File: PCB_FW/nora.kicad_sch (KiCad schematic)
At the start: 269 parts, among them J1 USB_C_Receptacle_USB2.0, J2 Conn_01x04, J3 Conn_01x02, J4 Conn_01x02, J5 Conn_02x03_Odd_Even, U1 ATmega32U4-MU, U2 24LC64, U4 Pico, Y1 16MHz

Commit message: フットプリントを整理
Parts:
- SW_1, SW_3: footprint Keebio-Parts:Kailh-PG1350-1u-MBK-WithKeyName-Socket-ForLeftEdge2 -> Keebio-Parts:Kailh-PG1350-1u-MBK-WithKeyName-Socket-ForLeftEdge
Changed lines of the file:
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@@
     (property "Reference" "SW_1" (id 0) (at 29.845 30.861 0))
     (property "Value" "ESC" (id 1) (at 29.845 33.1724 0))
-    (property "Footprint" "Keebio-Parts:Kailh-PG1350-1u-MBK-WithKeyName-Socket-ForLeftEdge2" (id 2) (at 29.845 33.02 0)
+    (property "Footprint" "Keebio-Parts:Kailh-PG1350-1u-MBK-WithKeyName-Socket-ForLeftEdge" (id 2) (at 29.845 33.02 0)
       (effects (font (size 1.27 1.27)) hide)
     )
@@
     (property "Reference" "SW_3" (id 0) (at 29.845 95.631 0))
     (property "Value" "LSFT" (id 1) (at 29.845 97.9424 0))
-    (property "Footprint" "Keebio-Parts:Kailh-PG1350-1u-MBK-WithKeyName-Socket-ForLeftEdge2" (id 2) (at 29.845 97.79 0)
+    (property "Footprint" "Keebio-Parts:Kailh-PG1350-1u-MBK-WithKeyName-Socket-ForLeftEdge" (id 2) (at 29.845 97.79 0)
       (effects (font (size 1.27 1.27)) hide)
     )
@@
     )
     (path "/00000000-0000-0000-0000-00005f6b0365"
-      (reference "SW_1") (unit 1) (value "ESC") (footprint "Keebio-Parts:Kailh-PG1350-1u-MBK-WithKeyName-Socket-ForLeftEdge2")
+      (reference "SW_1") (unit 1) (value "ESC") (footprint "Keebio-Parts:Kailh-PG1350-1u-MBK-WithKeyName-Socket-ForLeftEdge")
     )
     (path "/00000000-0000-0000-0000-000061ad1b1e"
-      (reference "SW_3") (unit 1) (value "LSFT") (footprint "Keebio-Parts:Kailh-PG1350-1u-MBK-WithKeyName-Socket-ForLeftEdge2")
+      (reference "SW_3") (unit 1) (value "LSFT") (footprint "Keebio-Parts:Kailh-PG1350-1u-MBK-WithKeyName-Socket-ForLeftEdge")
     )
     (path "/00000000-0000-0000-0000-000061aaf91e"

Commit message: Enlarge SW sub-hole? #68
1.7mmから1.8mmへ、5ピンの穴サイズを拡大
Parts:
- SW_1, SW_3: footprint Keebio-Parts:Kailh-PG1350-1u-MBK-WithKeyName-Socket-ForLeftEdge -> Keebio-Parts:Kailh-PG1350-1u-MBK-WithKeyName-Socket-ForLeftEdge-1.8mm-hole
- SW_10, SW_11, SW_12, SW_13, SW_15, SW_16, SW_17, SW_18, SW_20, SW_21, SW_22, SW_23, SW_24, SW_25, SW_26, SW_27, SW_28, SW_30, SW_31, SW_32, SW_33, SW_35, SW_36, SW_37, SW_38, SW_39, SW_40, SW_41, SW_42, SW_43, SW_44, SW_45, SW_46, SW_47, SW_48, SW_49, SW_5, SW_50, SW_51, SW_52, SW_53, SW_55, SW_56, SW_57, SW_58, SW_59, SW_60, SW_61, SW_62, SW_63, SW_65, SW_66, SW_67, SW_68, SW_70, SW_71, SW_72, SW_73, SW_75, SW_78, SW_8: footprint Keebio-Parts:Kailh-PG1350-1u-MBK-WithKeyName-Socket -> Keebio-Parts:Kailh-PG1350-1u-MBK-WithKeyName-Socket-1.8mm-hole
- SW_19, SW_29, SW_54, SW_6, SW_64, SW_7, SW_76, SW_77: footprint Keebio-Parts:Kailh-PG1350-1.5u-MBK-WithKeyName-Socket -> Keebio-Parts:Kailh-PG1350-1.5u-MBK-WithKeyName-Socket-1.8mm-hole

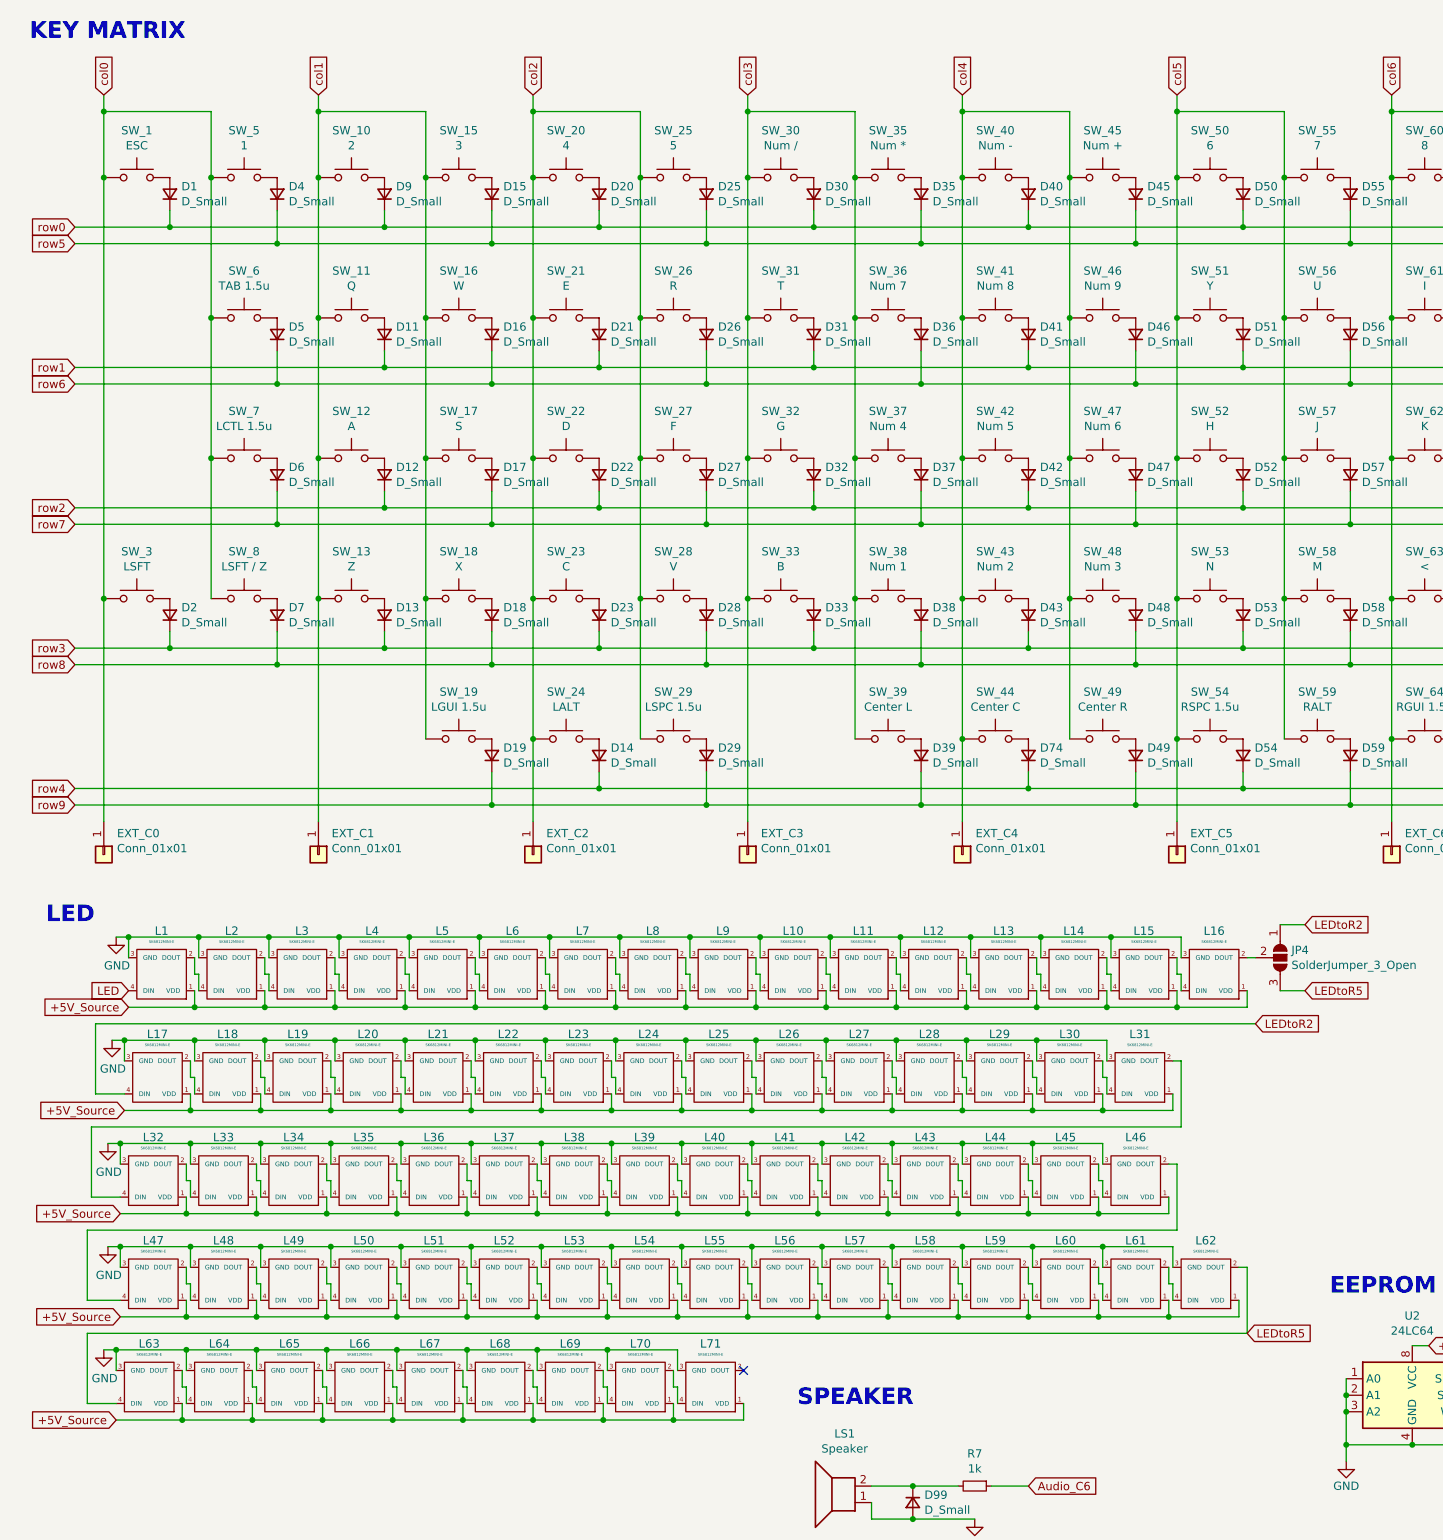
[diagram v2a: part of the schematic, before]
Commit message: WIP キー配置を調整中。LEDとキー減らしたところ
最下行を外に0.25uずらしたが、右下ネジ穴がソケットパッドに干渉するため、ずらすのをやめる。
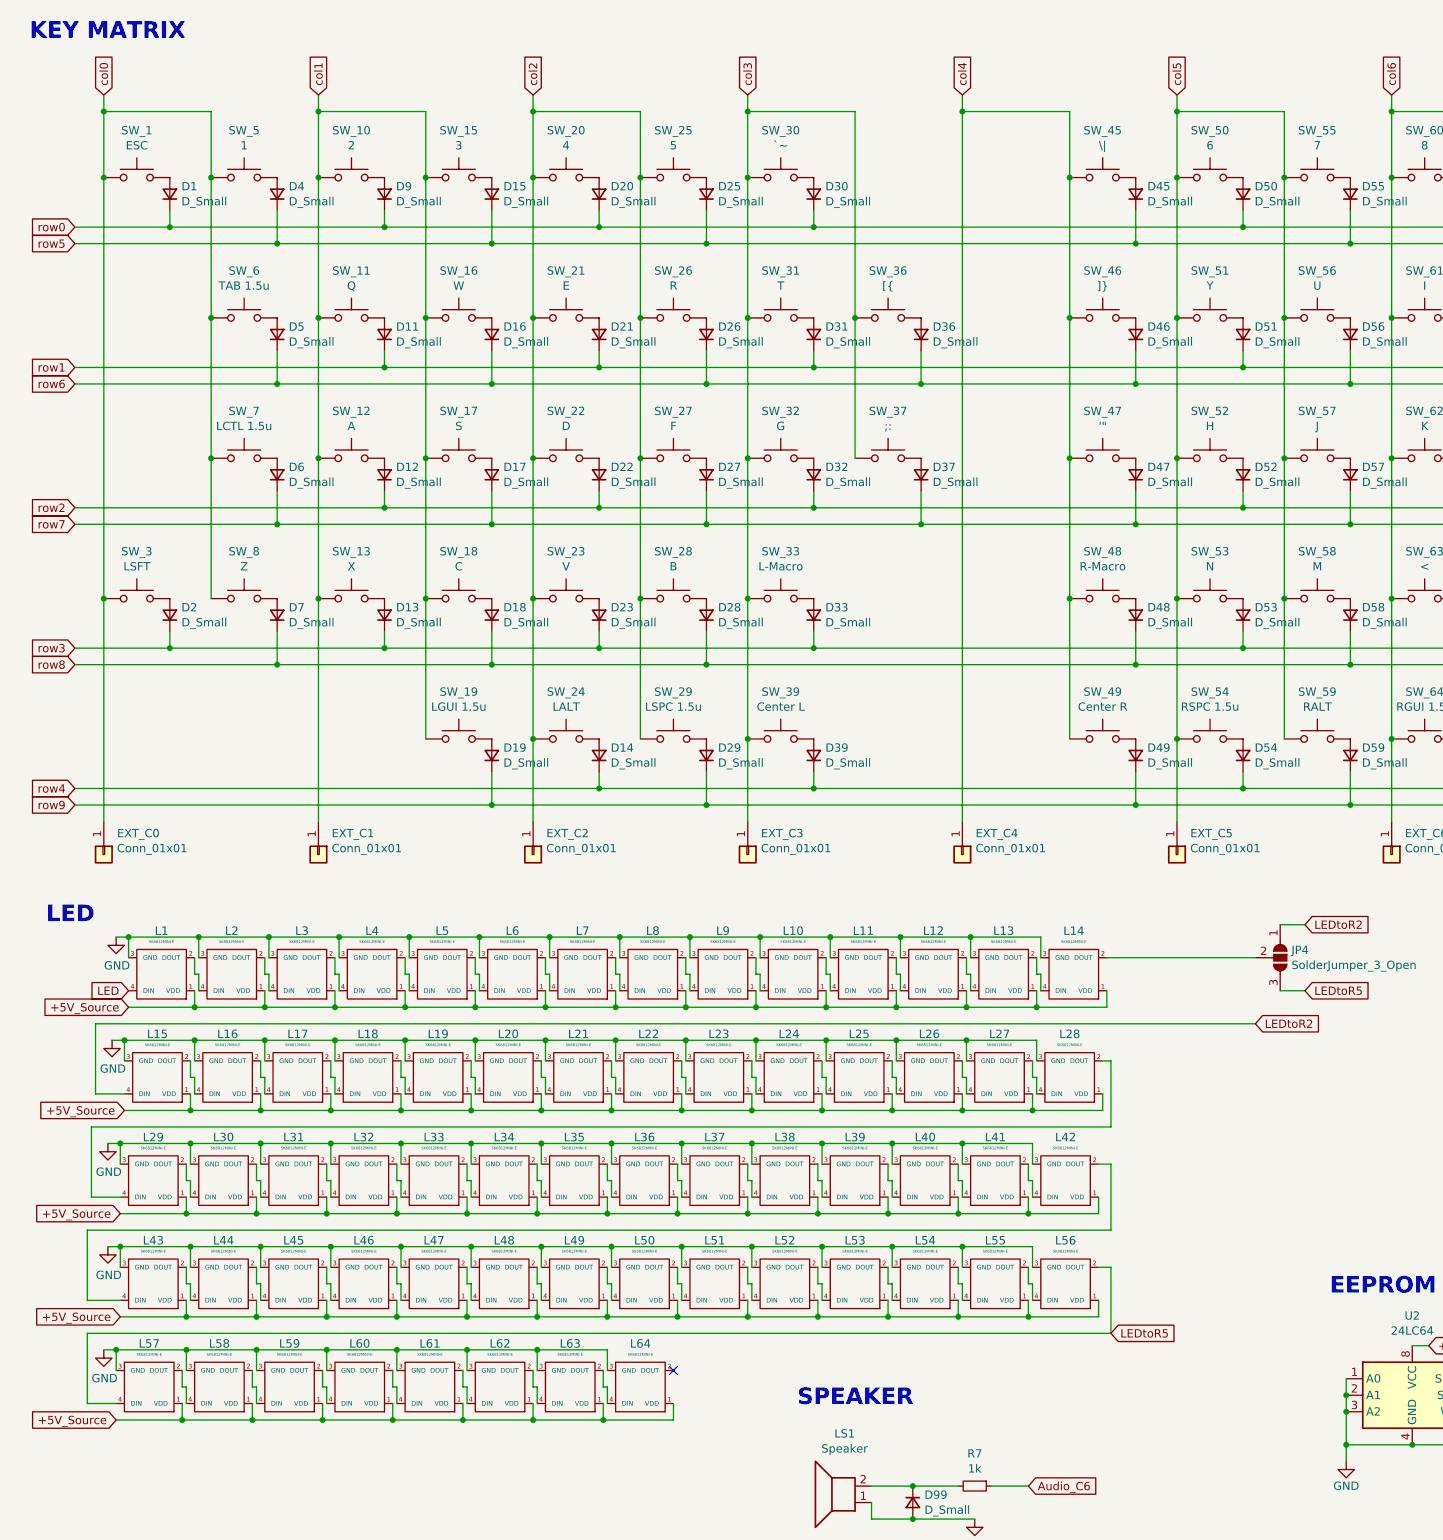
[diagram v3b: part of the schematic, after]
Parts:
- removed D35, D38, D40, D41, D42, D43, D74: D_Small, locallib:D_SOD-123-Pretty_No_Reference, symbol Device:D_Small
- removed L15, L16, L46, L71: SK6812MINI-E, Jones.local:YS-SK6812MINI-E_large_hole_with_reflection_paint_small_pad, symbol kbd:SK6812MINI-E
- removed L31, L61, L62: SK6812MINI-E, Jones.local:YS-SK6812MINI-E_large_hole_with_reflection_paint_small_pad_turned, symbol kbd:SK6812MINI-E
- removed SW_35: Num *, Keebio-Parts:Kailh-PG1350-1u-MBK-WithKeyName-Socket-1.8mm-hole, symbol Switch:SW_Push
- removed SW_38: Num 1, Keebio-Parts:Kailh-PG1350-1u-MBK-WithKeyName-Socket-1.8mm-hole, symbol Switch:SW_Push
- removed SW_40: Num -, Keebio-Parts:Kailh-PG1350-1u-MBK-WithKeyName-Socket-1.8mm-hole, symbol Switch:SW_Push
- removed SW_41: Num 8, Keebio-Parts:Kailh-PG1350-1u-MBK-WithKeyName-Socket-1.8mm-hole, symbol Switch:SW_Push
- removed SW_42: Num 5, Keebio-Parts:Kailh-PG1350-1u-MBK-WithKeyName-Socket-1.8mm-hole, symbol Switch:SW_Push
- removed SW_43: Num 2, Keebio-Parts:Kailh-PG1350-1u-MBK-WithKeyName-Socket-1.8mm-hole, symbol Switch:SW_Push
- removed SW_44: Center C, Keebio-Parts:Kailh-PG1350-1u-MBK-WithKeyName-Socket-1.8mm-hole, symbol Switch:SW_Push
- SW_13: value Z -> X
- SW_18: value X -> C
- SW_23: value C -> V
- SW_28: value V -> B
- SW_30: value Num / -> `~
- SW_33: value B -> L-Macro
- SW_36: value Num 7 -> [{
- SW_37: value Num 4 -> ;:
- SW_45: value Num + -> \|
- SW_46: value Num 9 -> ]}
- SW_47: value Num 6 -> '"
- SW_48: value Num 3 -> R-Macro
- SW_8: value LSFT / Z -> Z
- renumbered L17 to L15, L18 to L16, L19 to L17, L20 to L18, L21 to L19, L22 to L20, L23 to L21, L24 to L22, L25 to L23, L26 to L24, L27 to L25, L28 to L26, L29 to L27, L30 to L28, L32 to L29, L33 to L30, L34 to L31, L35 to L32, L36 to L33, L37 to L34, L38 to L35, L39 to L36, L40 to L37, L41 to L38, L42 to L39, L43 to L40, L44 to L41, L45 to L42, L47 to L43, L48 to L44, L49 to L45, L50 to L46, L51 to L47, L52 to L48, L53 to L49, L54 to L50, L55 to L51, L56 to L52, L57 to L53, L58 to L54, L59 to L55, L60 to L56, L63 to L57, L64 to L58, L65 to L59, L66 to L60, L67 to L61, L68 to L62, L69 to L63, L70 to L64
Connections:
- net LEDtoR5: now also L56.2 (DOUT)
- net row4: now also D39.1 (K)
- net row9: no longer D39.1 (K)
- net at L28.2 (DOUT): now also L29.4 (DIN)
- net at L42.2 (DOUT): now also L43.4 (DIN)
- net at L14.2 (DOUT): now also JP4.2 (C)
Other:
- moved on the sheet: D39, SW_39

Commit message: move LED reflection silk from LED to SW footprint #74
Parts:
- L1, L10, L11, L12, L13, L14, L2, L29, L3, L30, L31, L32, L33, L34, L35, L36, L37, L38, L39, L4, L40, L41, L42, L5, L57, L58, L59, L6, L60, L61, L62, L63, L64, L7, L8, L9: footprint Jones.local:YS-SK6812MINI-E_large_hole_with_reflection_paint_small_pad -> Jones.local:YS-SK6812MINI-E_large_hole_with_small_pad
- L15, L16, L17, L18, L19, L20, L21, L22, L23, L24, L25, L26, L27, L28, L43, L44, L45, L46, L47, L48, L49, L50, L51, L52, L53, L54, L55, L56: footprint Jones.local:YS-SK6812MINI-E_large_hole_with_reflection_paint_small_pad_turned -> Jones.local:YS-SK6812MINI-E_large_hole_with_small_pad
- SW_1, SW_3: footprint Keebio-Parts:Kailh-PG1350-1u-MBK-WithKeyName-Socket-ForLeftEdge-1.8mm-hole -> Keebio-Parts:Kailh-PG1350-1u-MBK-WithKeyName-Socket-ForLeftEdge-1.8mm-hole-reflection
- SW_10, SW_11, SW_12, SW_13, SW_15, SW_16, SW_17, SW_18, SW_20, SW_21, SW_22, SW_23, SW_24, SW_25, SW_26, SW_27, SW_28, SW_30, SW_31, SW_32, SW_33, SW_36, SW_37, SW_39, SW_45, SW_46, SW_47, SW_48, SW_49, SW_5, SW_50, SW_51, SW_52, SW_53, SW_55, SW_56, SW_57, SW_58, SW_59, SW_60, SW_61, SW_62, SW_63, SW_65, SW_66, SW_67, SW_68, SW_70, SW_71, SW_72, SW_73, SW_75, SW_78, SW_8: footprint Keebio-Parts:Kailh-PG1350-1u-MBK-WithKeyName-Socket-1.8mm-hole -> Keebio-Parts:Kailh-PG1350-1u-MBK-WithKeyName-Socket-1.8mm-hole-reflection
- SW_19, SW_29, SW_54, SW_6, SW_64, SW_7, SW_76, SW_77: footprint Keebio-Parts:Kailh-PG1350-1.5u-MBK-WithKeyName-Socket-1.8mm-hole -> Keebio-Parts:Kailh-PG1350-1.5u-MBK-WithKeyName-Socket-1.8mm-hole-reflection

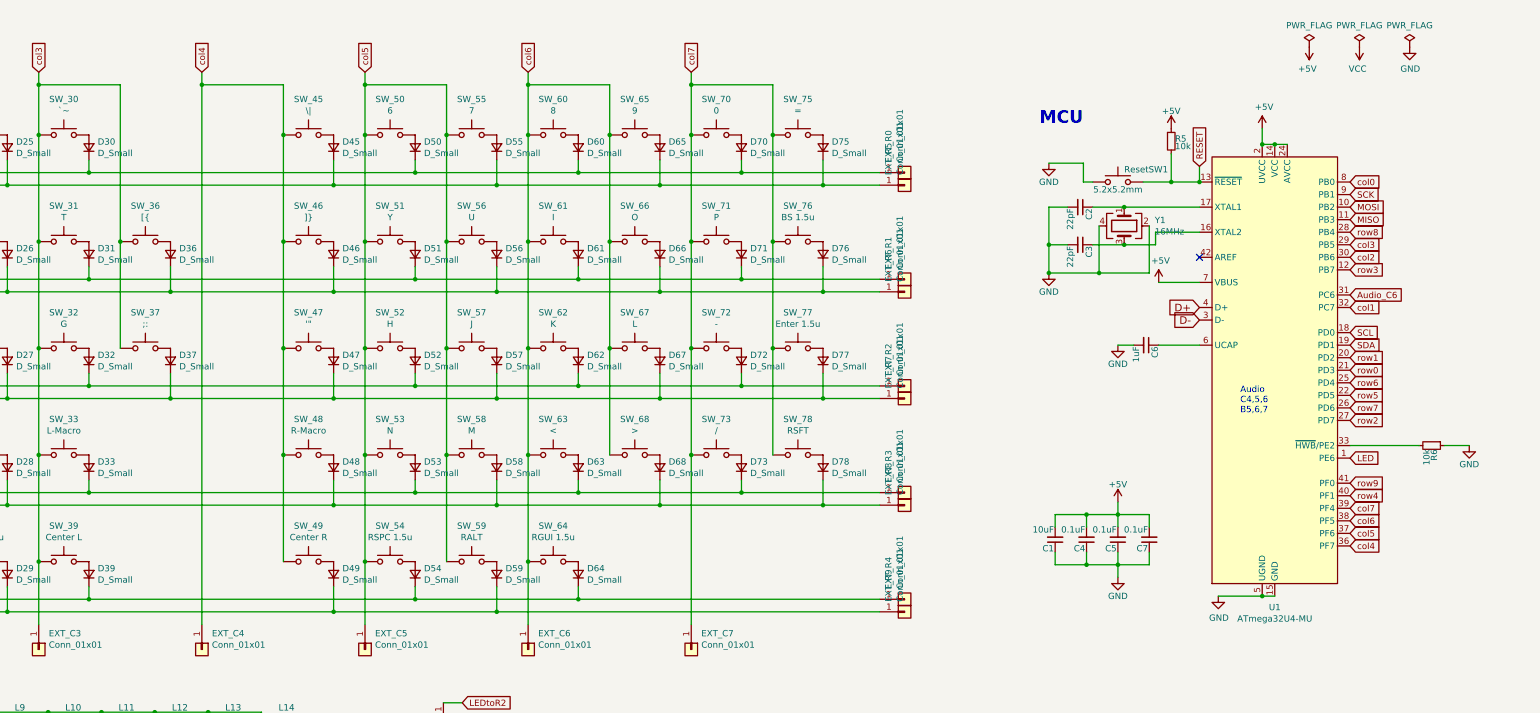
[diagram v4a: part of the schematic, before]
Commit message: WIP REを配置
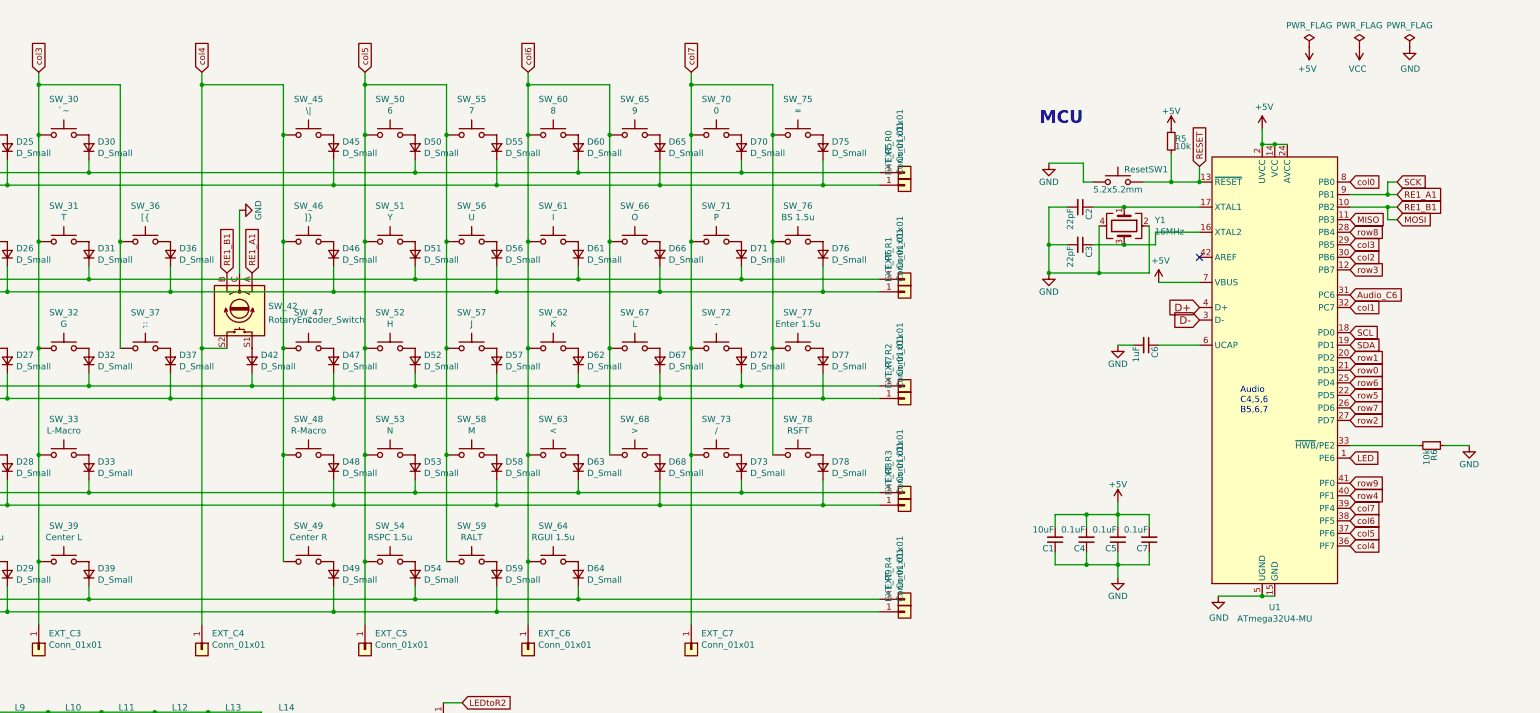
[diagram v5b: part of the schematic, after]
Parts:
- added D42: D_Small, locallib:D_SOD-123-Pretty_No_Reference, symbol Device:D_Small
- added SW_42: RotaryEncoder_Switch, locallib:RotaryEncoder_Alps_EC11K-Switch_Vertical_H20mm, symbol Device:RotaryEncoder_Switch
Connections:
- net GND: now also SW_42.C
- net MOSI: now also SW_42.B
- net col4: now also SW_42.S2
- net row2: now also D42.1 (K)
- net SCK renamed RE1_A1
- net RE1_A1: now also SW_42.A
- new net: D42.2 (A), SW_42.S1

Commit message: WIP とりあえず全キー埋め。なんとかなるような気がする
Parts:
- added D35, D38, D40, D41, D43, D44: D_Small, locallib:D_SOD-123-Pretty_No_Reference, symbol Device:D_Small
- added SW_35: R1L, Keebio-Parts:Kailh-PG1350-1u-MBK-WithKeyName-Socket-1.8mm-hole-reflection, symbol Switch:SW_Push
- added SW_38: R4L, Keebio-Parts:Kailh-PG1350-1u-MBK-WithKeyName-Socket-1.8mm-hole-reflection, symbol Switch:SW_Push
- added SW_40: R1R, Keebio-Parts:Kailh-PG1350-1u-MBK-WithKeyName-Socket-1.8mm-hole-reflection, symbol Switch:SW_Push
- added SW_41: R2C, Keebio-Parts:Kailh-PG1350-1u-MBK-WithKeyName-Socket-1.8mm-hole-reflection, symbol Switch:SW_Push
- added SW_42: R3C, Keebio-Parts:Kailh-PG1350-1u-MBK-WithKeyName-Socket-1.8mm-hole-reflection, symbol Switch:SW_Push
- added SW_43: R4R, Keebio-Parts:Kailh-PG1350-1u-MBK-WithKeyName-Socket-1.8mm-hole-reflection, symbol Switch:SW_Push
- added SW_44: Center 1.5u, Keebio-Parts:Kailh-PG1350-1.5u-MBK-WithKeyName-Socket-1.8mm-hole-reflection, symbol Switch:SW_Push
- renumbered SW_42 to RE_42
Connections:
- net col3: now also SW_35.1, SW_38.1
- net row0: now also D40.1 (K)
- net row1: now also D41.1 (K)
- net row3: now also D43.1 (K)
- net row4: now also D44.1 (K)
- net row5: now also D35.1 (K)
- net row8: now also D38.1 (K)
- net at D42.2 (A): now also SW_42.2; no longer RE_42.S1
- net RE1_A1 renamed SCK
- net col4 renamed RE1_S1
- net RE1_S1: now also RE_42.S1, SW_40.1, SW_41.1, SW_42.1, SW_43.1, SW_44.1; no longer RE_42.S2
- new net: D35.2 (A), SW_35.2
- new net: D40.2 (A), SW_40.2
- new net: D41.2 (A), SW_41.2
- new net: D38.2 (A), SW_38.2
- new net: D44.2 (A), SW_44.2
- new net RE1_S2: D43.2 (A), RE_42.S2, SW_43.2
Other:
- note added: "I2C PULL-UP"
- note added: "POWER SOURCE"
- note added: "ROTARY ENCODER"
- note removed: "Power Source for devices"
- moved on the sheet: RE_42

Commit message: WIP
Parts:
- added L15, L16, L31, L46, L61, L62, L71: SK6812MINI-E, Jones.local:YS-SK6812MINI-E_large_hole_with_small_pad, symbol kbd:SK6812MINI-E
- renumbered L15 to L17, L16 to L18, L17 to L19, L18 to L20, L19 to L21, L20 to L22, L21 to L23, L22 to L24, L23 to L25, L24 to L26, L25 to L27, L26 to L28, L27 to L29, L28 to L30, L29 to L32, L30 to L33, L31 to L34, L32 to L35, L33 to L36, L34 to L37, L35 to L38, L36 to L39, L37 to L40, L38 to L41, L39 to L42, L40 to L43, L41 to L44, L42 to L45, L43 to L47, L44 to L48, L45 to L49, L46 to L50, L47 to L51, L48 to L52, L49 to L53, L50 to L54, L51 to L55, L52 to L56, L53 to L57, L54 to L58, L55 to L59, L56 to L60, L57 to L63, L58 to L64, L59 to L65, L60 to L66, L61 to L67, L62 to L68, L63 to L69, L64 to L70
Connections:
- net +5V_Source: now also L15.1 (VDD), L16.1 (VDD), L31.1 (VDD), L46.1 (VDD), L61.1 (VDD), L62.1 (VDD), L71.1 (VDD)
- net GND: now also L15.3 (GND), L16.3 (GND), L31.3 (GND), L46.3 (GND), L61.3 (GND), L62.3 (GND), L71.3 (GND)
- net LEDtoR5: now also L62.2 (DOUT); no longer L60.2 (DOUT)
- net at L30.2 (DOUT): now also L31.4 (DIN); no longer L32.4 (DIN)
- net at L45.2 (DOUT): now also L46.4 (DIN); no longer L47.4 (DIN)
- net at L70.2 (DOUT): now also L71.4 (DIN)
- net at L14.2 (DOUT): now also L15.4 (DIN); no longer JP4.2 (C)
- new net: L31.2 (DOUT), L32.4 (DIN)
- new net: L46.2 (DOUT), L47.4 (DIN)
- new net: L60.2 (DOUT), L61.4 (DIN)
- new net: JP4.2 (C), L16.2 (DOUT)
- new net: L15.2 (DOUT), L16.4 (DIN)
- new net: L61.2 (DOUT), L62.4 (DIN)
